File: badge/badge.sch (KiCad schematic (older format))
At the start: 9 parts, among them K1 KEYSW, K2 KEYSW, K3 KEYSW, K4 KEYSW, U1 ProMicro

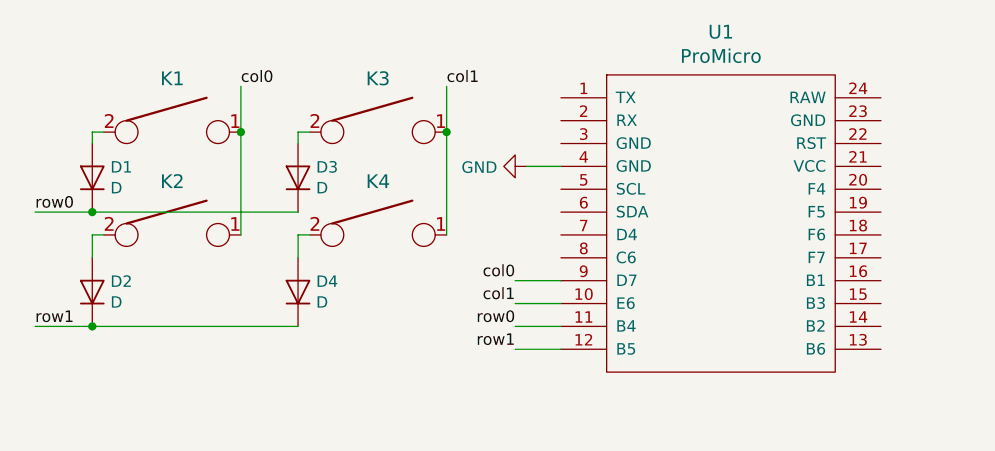
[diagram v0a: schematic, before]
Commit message: Cleanup routing, position logos relatively
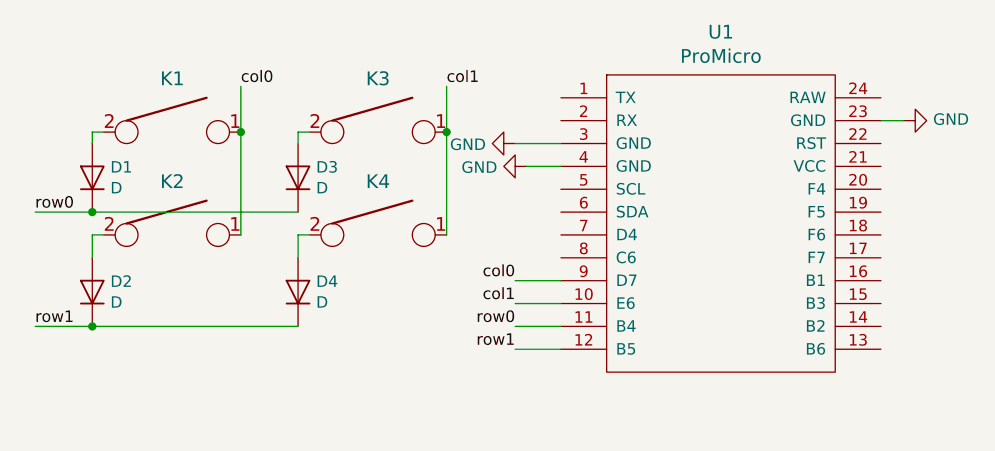
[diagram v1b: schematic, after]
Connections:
- net GND: now also U1.23 (GND), U1.3 (GND)
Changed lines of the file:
@@
 EESchema Schematic File Version 4
+LIBS:badge-cache
 EELAYER 26 0
 EELAYER END
@@
 Wire Wire Line
 	2950 1250 3100 1250
+$Comp
+L power:GND #PWR?
+U 1 1 5CD8AC7F
+P 2900 1150
+F 0 "#PWR?" H 2900 900 50  0001 C CNN
+F 1 "GND" V 2905 1022 50  0000 R CNN
+F 2 "" H 2900 1150 50  0001 C CNN
+F 3 "" H 2900 1150 50  0001 C CNN
+	1    2900 1150
+	0    1    1    0
+$EndComp
+$Comp
+L power:GND #PWR?
+U 1 1 5CD8ACC5
+P 4600 1050
+F 0 "#PWR?" H 4600 800 50  0001 C CNN
+F 1 "GND" V 4605 922 50  0000 R CNN
+F 2 "" H 4600 1050 50  0001 C CNN
+F 3 "" H 4600 1050 50  0001 C CNN
+	1    4600 1050
+	0    -1   -1   0
+$EndComp
+Wire Wire Line
+	4500 1050 4600 1050
+Wire Wire Line
+	3100 1150 2900 1150
 $EndSCHEMATC

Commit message: Use different pro micro pins for easier routing
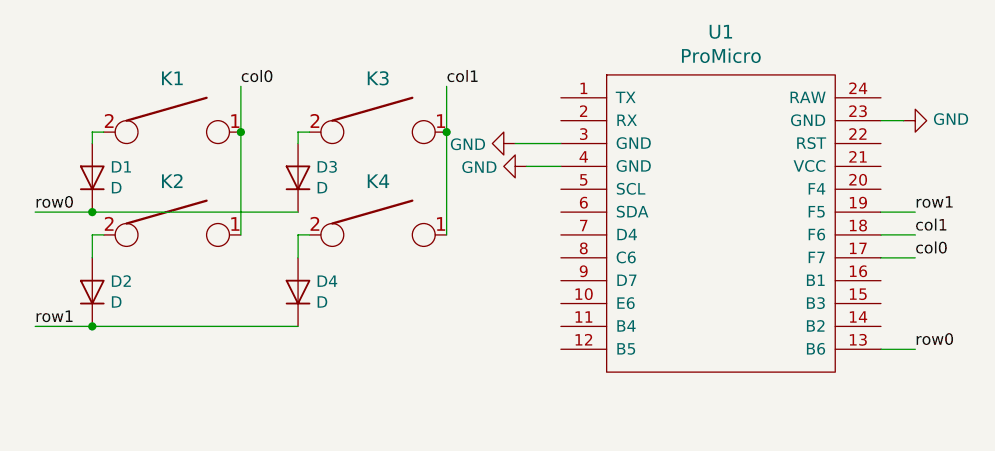
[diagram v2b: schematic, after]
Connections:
- net col0: now also U1.17 (F7); no longer U1.9 (D7)
- net col1: now also U1.18 (F6); no longer U1.10 (E6)
- net row0: now also U1.13 (B6); no longer U1.11 (B4)
- net row1: now also U1.19 (F5); no longer U1.12 (B5)
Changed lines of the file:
@@
 	1050 1950 800  1950
 Connection ~ 1050 1950
-Text Label 2900 1750 2    50   ~ 0
-col0
-Text Label 2900 1850 2    50   ~ 0
-col1
-Text Label 2900 1950 2    50   ~ 0
-row0
-Text Label 2900 2050 2    50   ~ 0
-row1
-Wire Wire Line
-	2900 1750 3100 1750
-Wire Wire Line
-	3100 1850 2900 1850
-Wire Wire Line
-	2900 1950 3100 1950
-Wire Wire Line
-	2900 2050 3100 2050
 $Comp
 L power:GND #PWR0101
@@
 	2950 1250 3100 1250
 $Comp
-L power:GND #PWR?
+L power:GND #PWR0102
 U 1 1 5CD8AC7F
 P 2900 1150
-F 0 "#PWR?" H 2900 900 50  0001 C CNN
+F 0 "#PWR0102" H 2900 900 50  0001 C CNN
 F 1 "GND" V 2905 1022 50  0000 R CNN
 F 2 "" H 2900 1150 50  0001 C CNN
@@
 $EndComp
 $Comp
-L power:GND #PWR?
+L power:GND #PWR0103
 U 1 1 5CD8ACC5
 P 4600 1050
-F 0 "#PWR?" H 4600 800 50  0001 C CNN
+F 0 "#PWR0103" H 4600 800 50  0001 C CNN
 F 1 "GND" V 4605 922 50  0000 R CNN
 F 2 "" H 4600 1050 50  0001 C CNN
@@
 Wire Wire Line
 	3100 1150 2900 1150
+Text Label 4650 1650 0    50   ~ 0
+col0
+Text Label 4650 1550 0    50   ~ 0
+col1
+Text Label 4650 2050 0    50   ~ 0
+row0
+Text Label 4650 1450 0    50   ~ 0
+row1
+Wire Wire Line
+	4500 1550 4650 1550
+Wire Wire Line
+	4650 1650 4500 1650
+Wire Wire Line
+	4500 2050 4650 2050
+Wire Wire Line
+	4650 1450 4500 1450
 $EndSCHEMATC

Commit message: Use SparkFun library, the keebs pro micro is wrong
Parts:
- U1: footprint keebs:Pro_Micro -> sparkfun_boards:SPARKFUN_PRO_MICRO; symbol promicro:ProMicro -> sparkfun_boards:SPARKFUN_PRO_MICRO
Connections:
- net col0: now also U1.19 (A2); no longer U1.17 (F7)
- net row1: now also U1.17 (A0); no longer U1.19 (F5)
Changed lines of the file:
@@
 EESchema Schematic File Version 4
 LIBS:badge-cache
-EELAYER 26 0
+EELAYER 29 0
 EELAYER END
 $Descr A4 11693 8268
@@
 $EndDescr
 $Comp
+L keyboard_parts:KEYSW K2
+U 1 1 5CD4EF89
+P 1400 1550
+F 0 "K2" H 1400 1783 60  0000 C CNN
+F 1 "KEYSW" H 1400 1450 60  0001 C CNN
+F 2 "keebs:Mx_Alps_100" H 1400 1550 60  0001 C CNN
+F 3 "" H 1400 1550 60  0000 C CNN
+	1    1400 1550
+	1    0    0    -1
+$EndComp
+$Comp
+L keyboard_parts:KEYSW K4
+U 1 1 5CD4EFCA
+P 2300 1550
+F 0 "K4" H 2300 1783 60  0000 C CNN
+F 1 "KEYSW" H 2300 1450 60  0001 C CNN
+F 2 "keebs:Mx_Alps_100" H 2300 1550 60  0001 C CNN
+F 3 "" H 2300 1550 60  0000 C CNN
+	1    2300 1550
+	1    0    0    -1
+$EndComp
+$Comp
+L Device:D D1
+U 1 1 5CD4F0CC
+P 1050 1300
+F 0 "D1" V 1096 1221 50  0000 R CNN
+F 1 "D" V 1005 1221 50  0000 R CNN
+F 2 "keyboard_parts:D_SOD123_axial" H 1050 1300 50  0001 C CNN
+F 3 "~" H 1050 1300 50  0001 C CNN
+	1    1050 1300
+	0    -1   -1   0
+$EndComp
+$Comp
+L Device:D D2
+U 1 1 5CD4F130
+P 1050 1800
+F 0 "D2" V 1096 1721 50  0000 R CNN
+F 1 "D" V 1005 1721 50  0000 R CNN
+F 2 "keyboard_parts:D_SOD123_axial" H 1050 1800 50  0001 C CNN
+F 3 "~" H 1050 1800 50  0001 C CNN
+	1    1050 1800
+	0    -1   -1   0
+$EndComp
+$Comp
+L Device:D D4
+U 1 1 5CD4F1B8
+P 1950 1800
+F 0 "D4" V 1996 1721 50  0000 R CNN
+F 1 "D" V 1905 1721 50  0000 R CNN
+F 2 "keyboard_parts:D_SOD123_axial" H 1950 1800 50  0001 C CNN
+F 3 "~" H 1950 1800 50  0001 C CNN
+	1    1950 1800
+	0    -1   -1   0
+$EndComp
+$Comp
+L Device:D D3
+U 1 1 5CD4F221
+P 1950 1300
+F 0 "D3" V 1996 1221 50  0000 R CNN
+F 1 "D" V 1905 1221 50  0000 R CNN
+F 2 "keyboard_parts:D_SOD123_axial" H 1950 1300 50  0001 C CNN
+F 3 "~" H 1950 1300 50  0001 C CNN
+	1    1950 1300
+	0    -1   -1   0
+$EndComp
+Wire Wire Line
+	1050 1150 1050 1100
+Wire Wire Line
+	1050 1100 1100 1100
+Wire Wire Line
+	1950 1150 1950 1100
+Wire Wire Line
+	1950 1100 2000 1100
+Wire Wire Line
+	1050 1450 1950 1450
+Wire Wire Line
+	1050 1650 1050 1550
+Wire Wire Line
+	1050 1550 1100 1550
+Wire Wire Line
+	1050 1950 1950 1950
+Wire Wire Line
+	1950 1650 1950 1550
+Wire Wire Line
+	1950 1550 2000 1550
+$Comp
+L sparkfun_boards:SPARKFUN_PRO_MICRO U1
+U 1 1 5CD4F6A0
+P 3800 1700
+F 0 "U1" H 3800 2737 60  0000 C CNN
+F 1 "ProMicro" H 3800 2631 60  0000 C CNN
+F 2 "sparkfun_boards:SPARKFUN_PRO_MICRO" H 3900 650 60  0001 C CNN
+F 3 "" H 3900 650 60  0000 C CNN
+	1    3800 1700
+	1    0    0    -1
+$EndComp
+Text Label 1700 900  0    50   ~ 0
+col0
+Text Label 2600 900  0    50   ~ 0
+col1
+Text Label 800  1450 0    50   ~ 0
+row0
+Text Label 800  1950 0    50   ~ 0
+row1
+Wire Wire Line
+	1050 1450 800  1450
+Connection ~ 1050 1450
+Wire Wire Line
+	1050 1950 800  1950
+Connection ~ 1050 1950
+$Comp
+L power:GND #PWR0101
+U 1 1 5CD559FA
+P 3100 1450
+F 0 "#PWR0101" H 3100 1200 50  0001 C CNN
+F 1 "GND" V 3105 1322 50  0000 R CNN
+F 2 "" H 3100 1450 50  0001 C CNN
+F 3 "" H 3100 1450 50  0001 C CNN
+	1    3100 1450
+	0    1    1    0
+$EndComp
+$Comp
+L power:GND #PWR0102
+U 1 1 5CD8AC7F
+P 3050 1350
+F 0 "#PWR0102" H 3050 1100 50  0001 C CNN
+F 1 "GND" V 3055 1222 50  0000 R CNN
+F 2 "" H 3050 1350 50  0001 C CNN
+F 3 "" H 3050 1350 50  0001 C CNN
+	1    3050 1350
+	0    1    1    0
+$EndComp
+$Comp
+L power:GND #PWR0103
+U 1 1 5CD8ACC5
+P 4350 1250
+F 0 "#PWR0103" H 4350 1000 50  0001 C CNN
+F 1 "GND" V 4355 1122 50  0000 R CNN
+F 2 "" H 4350 1250 50  0001 C CNN
+F 3 "" H 4350 1250 50  0001 C CNN
+	1    4350 1250
+	0    -1   -1   0
+$EndComp
+Wire Wire Line
+	4250 1250 4350 1250
+Text Label 4400 1650 0    50   ~ 0
+col0
+Text Label 4400 1750 0    50   ~ 0
+col1
+Text Label 4400 2250 0    50   ~ 0
+row0
+Wire Wire Line
+	4250 1750 4400 1750
+Wire Wire Line
+	4400 1650 4250 1650
+Wire Wire Line
+	4250 2250 4400 2250
+Wire Wire Line
+	3050 1350 3350 1350
+Wire Wire Line
+	3100 1450 3350 1450
+Wire Wire Line
+	4400 1850 4250 1850
+Text Label 4400 1850 0    50   ~ 0
+row1
+$Comp
 L keyboard_parts:KEYSW K1
 U 1 1 5CD4EF09
@@
 	1    0    0    -1
 $EndComp
+Wire Wire Line
+	1700 900  1700 1100
+Wire Wire Line
+	1700 1100 1700 1550
+Connection ~ 1700 1100
 $Comp
 L keyboard_parts:KEYSW K3
@@
 	1    0    0    -1
 $EndComp
-$Comp
-L keyboard_parts:KEYSW K2
-U 1 1 5CD4EF89
-P 1400 1550
-F 0 "K2" H 1400 1783 60  0000 C CNN
-F 1 "KEYSW" H 1400 1450 60  0001 C CNN
-F 2 "keebs:Mx_Alps_100" H 1400 1550 60  0001 C CNN
-F 3 "" H 1400 1550 60  0000 C CNN
-	1    1400 1550
-	1    0    0    -1
-$EndComp
-$Comp
-L keyboard_parts:KEYSW K4
-U 1 1 5CD4EFCA
-P 2300 1550
-F 0 "K4" H 2300 1783 60  0000 C CNN
-F 1 "KEYSW" H 2300 1450 60  0001 C CNN
-F 2 "keebs:Mx_Alps_100" H 2300 1550 60  0001 C CNN
-F 3 "" H 2300 1550 60  0000 C CNN
-	1    2300 1550
-	1    0    0    -1
-$EndComp
-$Comp
-L Device:D D1
-U 1 1 5CD4F0CC
-P 1050 1300
-F 0 "D1" V 1096 1221 50  0000 R CNN
-F 1 "D" V 1005 1221 50  0000 R CNN
-F 2 "keyboard_parts:D_SOD123_axial" H 1050 1300 50  0001 C CNN
-F 3 "~" H 1050 1300 50  0001 C CNN
-	1    1050 1300
-	0    -1   -1   0
-$EndComp
-$Comp
-L Device:D D2
-U 1 1 5CD4F130
-P 1050 1800
-F 0 "D2" V 1096 1721 50  0000 R CNN
-F 1 "D" V 1005 1721 50  0000 R CNN
-F 2 "keyboard_parts:D_SOD123_axial" H 1050 1800 50  0001 C CNN
-F 3 "~" H 1050 1800 50  0001 C CNN
-	1    1050 1800
-	0    -1   -1   0
-$EndComp
-$Comp
-L Device:D D4
-U 1 1 5CD4F1B8
-P 1950 1800
-F 0 "D4" V 1996 1721 50  0000 R CNN
-F 1 "D" V 1905 1721 50  0000 R CNN
-F 2 "keyboard_parts:D_SOD123_axial" H 1950 1800 50  0001 C CNN
-F 3 "~" H 1950 1800 50  0001 C CNN
-	1    1950 1800
-	0    -1   -1   0
-$EndComp
-$Comp
-L Device:D D3
-U 1 1 5CD4F221
-P 1950 1300
-F 0 "D3" V 1996 1221 50  0000 R CNN
-F 1 "D" V 1905 1221 50  0000 R CNN
-F 2 "keyboard_parts:D_SOD123_axial" H 1950 1300 50  0001 C CNN
-F 3 "~" H 1950 1300 50  0001 C CNN
-	1    1950 1300
-	0    -1   -1   0
-$EndComp
-Wire Wire Line
-	1050 1150 1050 1100
-Wire Wire Line
-	1050 1100 1100 1100
-Wire Wire Line
-	1950 1150 1950 1100
-Wire Wire Line
-	1950 1100 2000 1100
-Wire Wire Line
-	1050 1450 1950 1450
-Wire Wire Line
-	1700 1100 1700 1550
-Wire Wire Line
-	1050 1650 1050 1550
-Wire Wire Line
-	1050 1550 1100 1550
-Wire Wire Line
-	1050 1950 1950 1950
-Wire Wire Line
-	1950 1650 1950 1550
-Wire Wire Line
-	1950 1550 2000 1550
+Wire Wire Line
+	2600 900  2600 1100
 Wire Wire Line
 	2600 1100 2600 1550
-$Comp
-L promicro:ProMicro U1
-U 1 1 5CD4F6A0
-P 3800 1700
-F 0 "U1" H 3800 2737 60  0000 C CNN
-F 1 "ProMicro" H 3800 2631 60  0000 C CNN
-F 2 "keebs:Pro_Micro" H 3900 650 60  0001 C CNN
-F 3 "" H 3900 650 60  0000 C CNN
-	1    3800 1700
-	1    0    0    -1
-$EndComp
-Text Label 1700 900  0    50   ~ 0
-col0
-Text Label 2600 900  0    50   ~ 0
-col1
-Text Label 800  1450 0    50   ~ 0
-row0
-Text Label 800  1950 0    50   ~ 0
-row1
-Wire Wire Line
-	1700 1100 1700 900
-Connection ~ 1700 1100
-Wire Wire Line
-	2600 1100 2600 900
 Connection ~ 2600 1100
-Wire Wire Line
-	1050 1450 800  1450
-Connection ~ 1050 1450
-Wire Wire Line
-	1050 1950 800  1950
-Connection ~ 1050 1950
-$Comp
-L power:GND #PWR0101
-U 1 1 5CD559FA
-P 2950 1250
-F 0 "#PWR0101" H 2950 1000 50  0001 C CNN
-F 1 "GND" V 2955 1122 50  0000 R CNN
-F 2 "" H 2950 1250 50  0001 C CNN
-F 3 "" H 2950 1250 50  0001 C CNN
-	1    2950 1250
-	0    1    1    0
-$EndComp
-Wire Wire Line
-	2950 1250 3100 1250
-$Comp
-L power:GND #PWR0102
-U 1 1 5CD8AC7F
-P 2900 1150
-F 0 "#PWR0102" H 2900 900 50  0001 C CNN
-F 1 "GND" V 2905 1022 50  0000 R CNN
-F 2 "" H 2900 1150 50  0001 C CNN
-F 3 "" H 2900 1150 50  0001 C CNN
-	1    2900 1150
-	0    1    1    0
-$EndComp
-$Comp
-L power:GND #PWR0103
-U 1 1 5CD8ACC5
-P 4600 1050
-F 0 "#PWR0103" H 4600 800 50  0001 C CNN
-F 1 "GND" V 4605 922 50  0000 R CNN
-F 2 "" H 4600 1050 50  0001 C CNN
-F 3 "" H 4600 1050 50  0001 C CNN
-	1    4600 1050
-	0    -1   -1   0
-$EndComp
-Wire Wire Line
-	4500 1050 4600 1050
-Wire Wire Line
-	3100 1150 2900 1150
-Text Label 4650 1650 0    50   ~ 0
-col0
-Text Label 4650 1550 0    50   ~ 0
-col1
-Text Label 4650 2050 0    50   ~ 0
-row0
-Text Label 4650 1450 0    50   ~ 0
-row1
-Wire Wire Line
-	4500 1550 4650 1550
-Wire Wire Line
-	4650 1650 4500 1650
-Wire Wire Line
-	4500 2050 4650 2050
-Wire Wire Line
-	4650 1450 4500 1450
 $EndSCHEMATC

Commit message: 2x3 layout and case
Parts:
- added D3, D6: D, keyboard_parts:D_SOD123_axial, symbol Device:D
- added K3, K6: KEYSW, keebs:Mx_Alps_100, symbol keyboard_parts:KEYSW
- renumbered D3 to D4, D4 to D5, K3 to K4, K4 to K5
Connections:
- net col0: now also U1.5 (2), K3.1; no longer U1.19 (A2)
- net col1: now also U1.10 (7), K6.1; no longer U1.18 (A1)
- net row0: now also U1.17 (A0); no longer U1.13 (*10)
- net row1: now also U1.13 (*10); no longer U1.17 (A0)
- net row2: now reaches U1.20 (A3)
- net row2: now also D3.1 (K), D6.1 (K)
- new net: D3.2 (A), K3.2
- new net: D6.2 (A), K6.2
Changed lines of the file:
@@
 $EndComp
 $Comp
-L keyboard_parts:KEYSW K4
+L keyboard_parts:KEYSW K5
 U 1 1 5CD4EFCA
 P 2300 1550
-F 0 "K4" H 2300 1783 60  0000 C CNN
+F 0 "K5" H 2300 1783 60  0000 C CNN
 F 1 "KEYSW" H 2300 1450 60  0001 C CNN
 F 2 "keebs:Mx_Alps_100" H 2300 1550 60  0001 C CNN
@@
 $EndComp
 $Comp
-L Device:D D4
+L Device:D D5
 U 1 1 5CD4F1B8
 P 1950 1800
-F 0 "D4" V 1996 1721 50  0000 R CNN
+F 0 "D5" V 1996 1721 50  0000 R CNN
 F 1 "D" V 1905 1721 50  0000 R CNN
 F 2 "keyboard_parts:D_SOD123_axial" H 1950 1800 50  0001 C CNN
@@
 $EndComp
 $Comp
-L Device:D D3
+L Device:D D4
 U 1 1 5CD4F221
 P 1950 1300
-F 0 "D3" V 1996 1221 50  0000 R CNN
+F 0 "D4" V 1996 1221 50  0000 R CNN
 F 1 "D" V 1905 1221 50  0000 R CNN
 F 2 "keyboard_parts:D_SOD123_axial" H 1950 1300 50  0001 C CNN
@@
 Wire Wire Line
 	4250 1250 4350 1250
-Text Label 4400 1650 0    50   ~ 0
-col0
-Text Label 4400 1750 0    50   ~ 0
+Text Label 3350 2050 2    50   ~ 0
 col1
+Text Label 4400 1850 0    50   ~ 0
+row0
+Wire Wire Line
+	4250 2250 4400 2250
+Wire Wire Line
+	3050 1350 3350 1350
+Wire Wire Line
+	3100 1450 3350 1450
+Wire Wire Line
+	4400 1850 4250 1850
 Text Label 4400 2250 0    50   ~ 0
-row0
-Wire Wire Line
-	4250 1750 4400 1750
-Wire Wire Line
-	4400 1650 4250 1650
-Wire Wire Line
-	4250 2250 4400 2250
-Wire Wire Line
-	3050 1350 3350 1350
-Wire Wire Line
-	3100 1450 3350 1450
-Wire Wire Line
-	4400 1850 4250 1850
-Text Label 4400 1850 0    50   ~ 0
 row1
 $Comp
@@
 Connection ~ 1700 1100
 $Comp
-L keyboard_parts:KEYSW K3
+L keyboard_parts:KEYSW K4
 U 1 1 5CD4EF59
 P 2300 1100
-F 0 "K3" H 2300 1333 60  0000 C CNN
+F 0 "K4" H 2300 1333 60  0000 C CNN
 F 1 "KEYSW" H 2300 1000 60  0001 C CNN
 F 2 "keebs:Mx_Alps_100" H 2300 1100 60  0001 C CNN
@@
 	2600 1100 2600 1550
 Connection ~ 2600 1100
+$Comp
+L keyboard_parts:KEYSW K3
+U 1 1 5CEA56E1
+P 1400 2000
+F 0 "K3" H 1400 2233 60  0000 C CNN
+F 1 "KEYSW" H 1400 1900 60  0001 C CNN
+F 2 "keebs:Mx_Alps_100" H 1400 2000 60  0001 C CNN
+F 3 "" H 1400 2000 60  0000 C CNN
+	1    1400 2000
+	1    0    0    -1
+$EndComp
+$Comp
+L keyboard_parts:KEYSW K6
+U 1 1 5CEA5D9A
+P 2300 2000
+F 0 "K6" H 2300 2233 60  0000 C CNN
+F 1 "KEYSW" H 2300 1900 60  0001 C CNN
+F 2 "keebs:Mx_Alps_100" H 2300 2000 60  0001 C CNN
+F 3 "" H 2300 2000 60  0000 C CNN
+	1    2300 2000
+	1    0    0    -1
+$EndComp
+$Comp
+L Device:D D3
+U 1 1 5CEA64D8
+P 1050 2250
+F 0 "D3" V 1096 2171 50  0000 R CNN
+F 1 "D" V 1005 2171 50  0000 R CNN
+F 2 "keyboard_parts:D_SOD123_axial" H 1050 2250 50  0001 C CNN
+F 3 "~" H 1050 2250 50  0001 C CNN
+	1    1050 2250
+	0    -1   -1   0
+$EndComp
+$Comp
+L Device:D D6
+U 1 1 5CEA6B42
+P 1950 2250
+F 0 "D6" V 1996 2171 50  0000 R CNN
+F 1 "D" V 1905 2171 50  0000 R CNN
+F 2 "keyboard_parts:D_SOD123_axial" H 1950 2250 50  0001 C CNN
+F 3 "~" H 1950 2250 50  0001 C CNN
+	1    1950 2250
+	0    -1   -1   0
+$EndComp
+Wire Wire Line
+	1700 1550 1700 2000
+Connection ~ 1700 1550
+Wire Wire Line
+	2600 1550 2600 2000
+Connection ~ 2600 1550
+Wire Wire Line
+	2000 2000 1950 2000
+Wire Wire Line
+	1950 2000 1950 2100
+Wire Wire Line
+	1100 2000 1050 2000
+Wire Wire Line
+	1050 2000 1050 2100
+Wire Wire Line
+	1950 2400 1050 2400
+Text Label 950  2400 2    50   ~ 0
+row2
+Text Label 4400 1550 0    50   ~ 0
+row2
+Wire Wire Line
+	4400 1550 4250 1550
+Wire Wire Line
+	950  2400 1050 2400
+Connection ~ 1050 2400
+Text Label 3350 1550 2    50   ~ 0
+col0
 $EndSCHEMATC
